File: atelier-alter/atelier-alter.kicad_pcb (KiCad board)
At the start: 2 copper layers, 81.3 x 80 mm, 59 parts, among them SW1 SW_DPST, SW2 SW_DPST, SW3 SW_DPST, SW4 RESET, U1 ATmega32U4-A, U2 PRTR5V0U2X, Y1 16Mhz

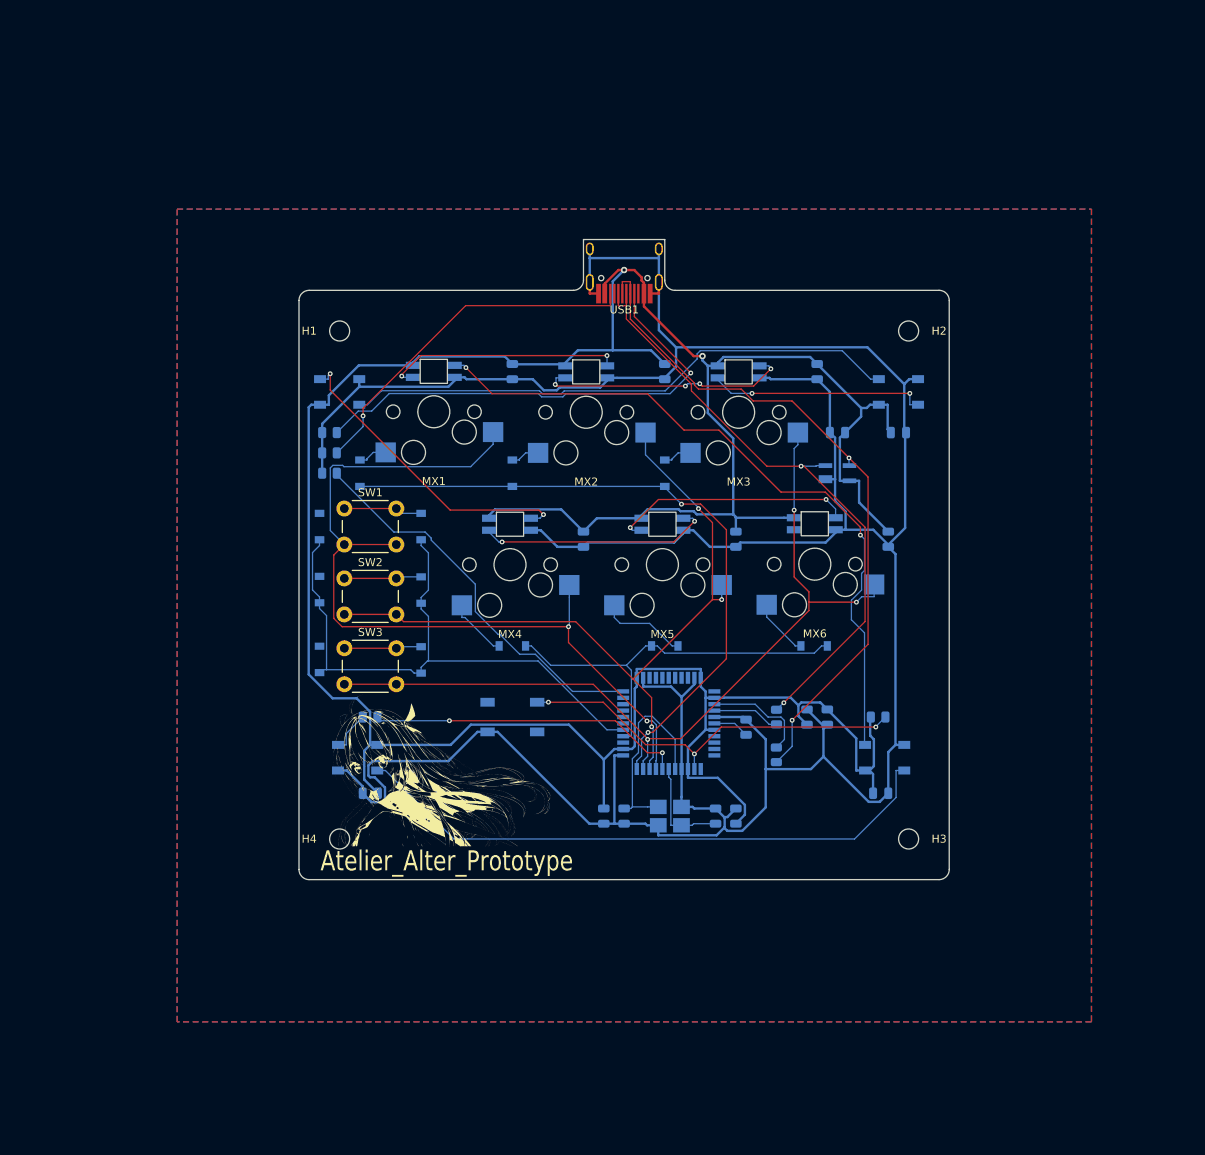
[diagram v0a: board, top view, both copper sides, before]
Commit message: small tweaks, done drawing the case
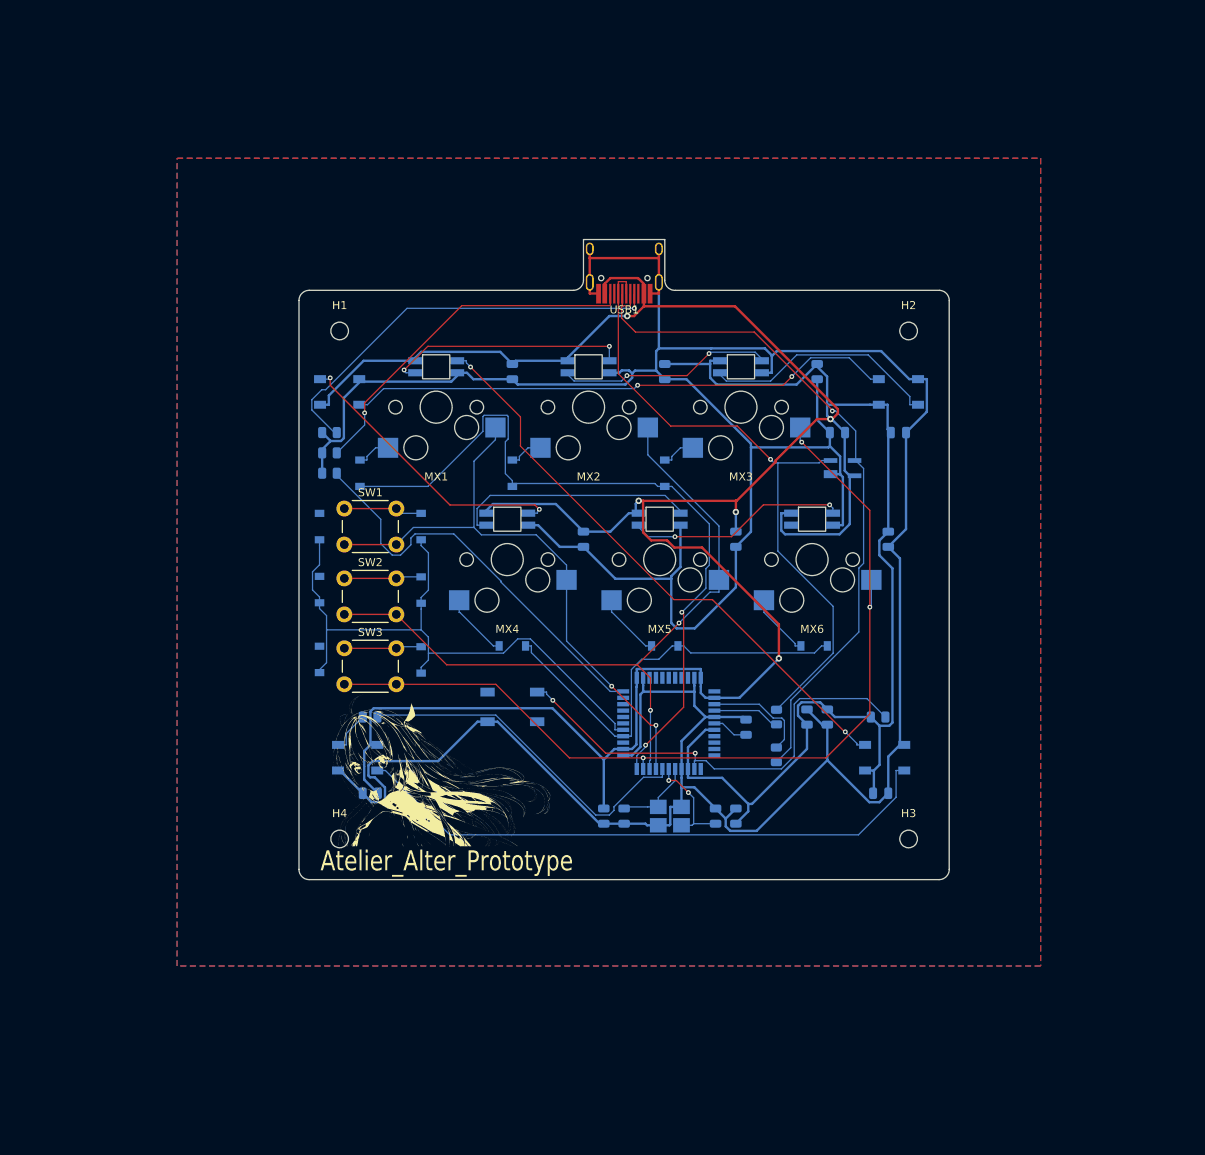
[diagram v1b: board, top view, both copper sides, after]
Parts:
- D14, D2, D5, D9: value SK6812 -> SK6812 / WS2812B; footprint LED_SMD:LED_SK6812_PLCC4_5.0x5.0mm_P3.2mm -> LED_SMD:LED_WS2812B_PLCC4_5.0x5.0mm_P3.2mm
- H1, H2, H3, H4: footprint MountingHole:MountingHole_2.5mm -> MountingHole:MountingHole_2.2mm_M2
- moved SW4 1.27 mm to (143.5, 113.0)
- moved U2 0.90 mm to (184.8, 83.2)
- moved MX4 0.72 mm to (142.9, 94.6)
- moved MX5 0.72 mm to (161.9, 94.6)
- moved MX3 0.70 mm to (172.1, 75.6)
- moved MX2 0.70 mm to (153.0, 75.6)
- moved MX6 0.67 mm to (181.0, 94.6)
- moved MX1 0.64 mm to (134.0, 75.6)
- turned D14 to 180 degrees
- turned D2 to 0 degrees
- turned D22 to 180 degrees
- turned D5 to 180 degrees
- turned D9 to 180 degrees
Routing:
- net +5V: track 378.2 -> 429.2 mm, vias 2 -> 5
- net COL1: track 107.6 -> 74.7 mm
- net GND: track 411.3 -> 443.9 mm
- net Net-(C3-Pad2): track 25.0 -> 9.96 mm
- net D11: track 87.9 -> 73.3 mm
- net COL3: track 104.7 -> 116.1 mm
- net ROW1: track 83.1 -> 93.9 mm
- net Net-(R4-Pad2): track 60.5 -> 52.4 mm
- net Net-(R3-Pad1): track 50.0 -> 57.7 mm, vias 3 -> 2
- net Net-(MX2-Pad3): track 31.9 -> 26.9 mm, vias 4 -> 2
- net RGB: track 39.5 -> 44.1 mm, vias 2 -> 0
- net D+: track 77.3 -> 81.9 mm, vias 2 -> 1
- net Net-(MX5-Pad3): track 30.3 -> 27.5 mm
- net Net-(D22-Pad2): track 11.0 -> 8.26 mm
- net ROW2: track 50.6 -> 53.2 mm
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
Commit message: minor updates here and there
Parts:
- removed D17, D18, D19: SOD-123, Diode_SMD:D_SOD-123
- H1, H2, H3, H4: footprint MountingHole:MountingHole_2.2mm_M2 -> MountingHole:MountingHole_5.3mm_M5
- moved R1 53.1 mm to (154.9, 70.5), turned to 0 degrees
- moved R2 46.9 mm to (159.7, 70.5), turned to 180 degrees
- moved R5 46.6 mm to (165.1, 67.3), turned to 90 degrees
- moved R6 45.5 mm to (154.9, 113.7), turned to 90 degrees
- moved U2 31.6 mm to (157.5, 67.3), turned to 180 degrees
- moved R4 31.4 mm to (149.9, 67.3), turned to 90 degrees
- moved D14 13.9 mm to (134.6, 67.9)
- moved D9 12.8 mm to (180.3, 67.9)
- moved Atorie' 12.1 mm to (146.7, 120.7)
- moved R7 12.0 mm to (129.3, 125.7)
- moved R3 11.4 mm to (185.4, 125.1)
- moved C10 8.76 mm to (134.3, 125.7)
- moved C11 8.67 mm to (181.0, 125.1), turned to 180 degrees
- moved D2 8.14 mm to (132.1, 121.3)
- moved SW4 7.43 mm to (146.1, 120.0)
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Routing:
- net GND: track 443.9 -> 371.1 mm
- net D-: track 87.2 -> 17.6 mm
- net D+: track 81.9 -> 13.3 mm
- net Net-(R6-Pad1): track 51.8 -> 2.49 mm
- net Net-(R3-Pad1): track 57.7 -> 106.6 mm, vias 2 -> 0
- net Net-(R2-Pad2): track 8.48 -> 53.7 mm, vias 0 -> 2
- net Net-(R1-Pad2): track 13.4 -> 52.9 mm, vias 0 -> 2
- net ROW3: track 78.3 -> 45.2 mm
- net Net-(R5-Pad2): track 44.9 -> 12.3 mm
- net Net-(R4-Pad2): track 52.4 -> 23.6 mm
- net Net-(D14-Pad2): track 68.5 -> 42.1 mm
- net Net-(D2-Pad4): track 74.5 -> 53.4 mm, vias 0 -> 2
- net ROW1: track 93.9 -> 73.7 mm, vias 2 -> 3
- net +5V: track 429.2 -> 442.5 mm, vias 5 -> 2
- net D12: track 29.9 -> 18.1 mm
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
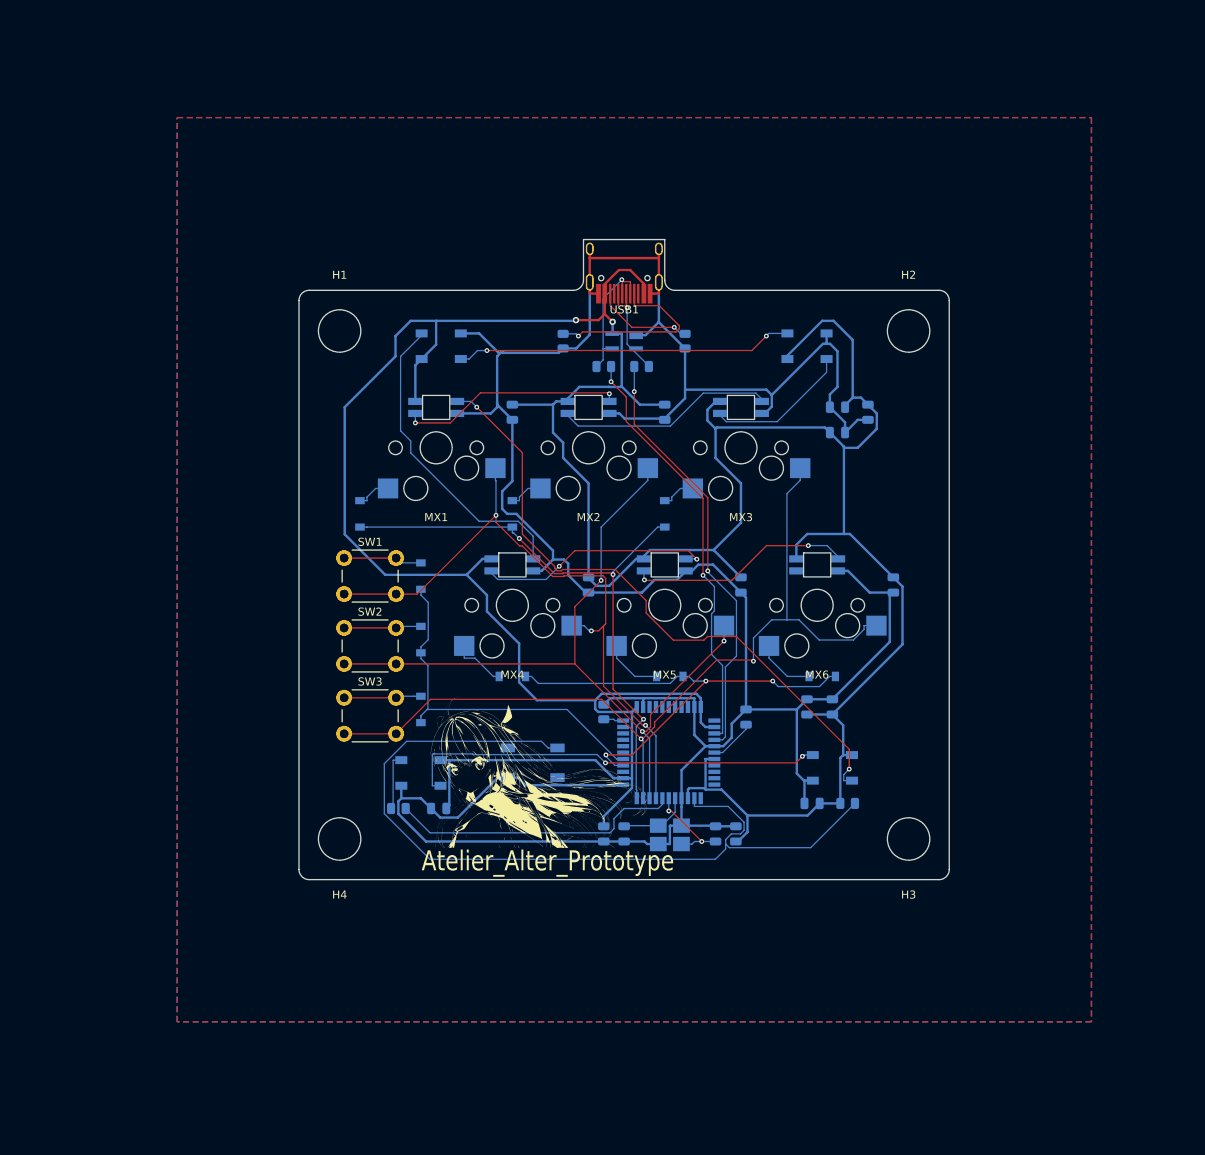
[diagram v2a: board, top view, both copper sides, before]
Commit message: decided to nuke all led capacitor
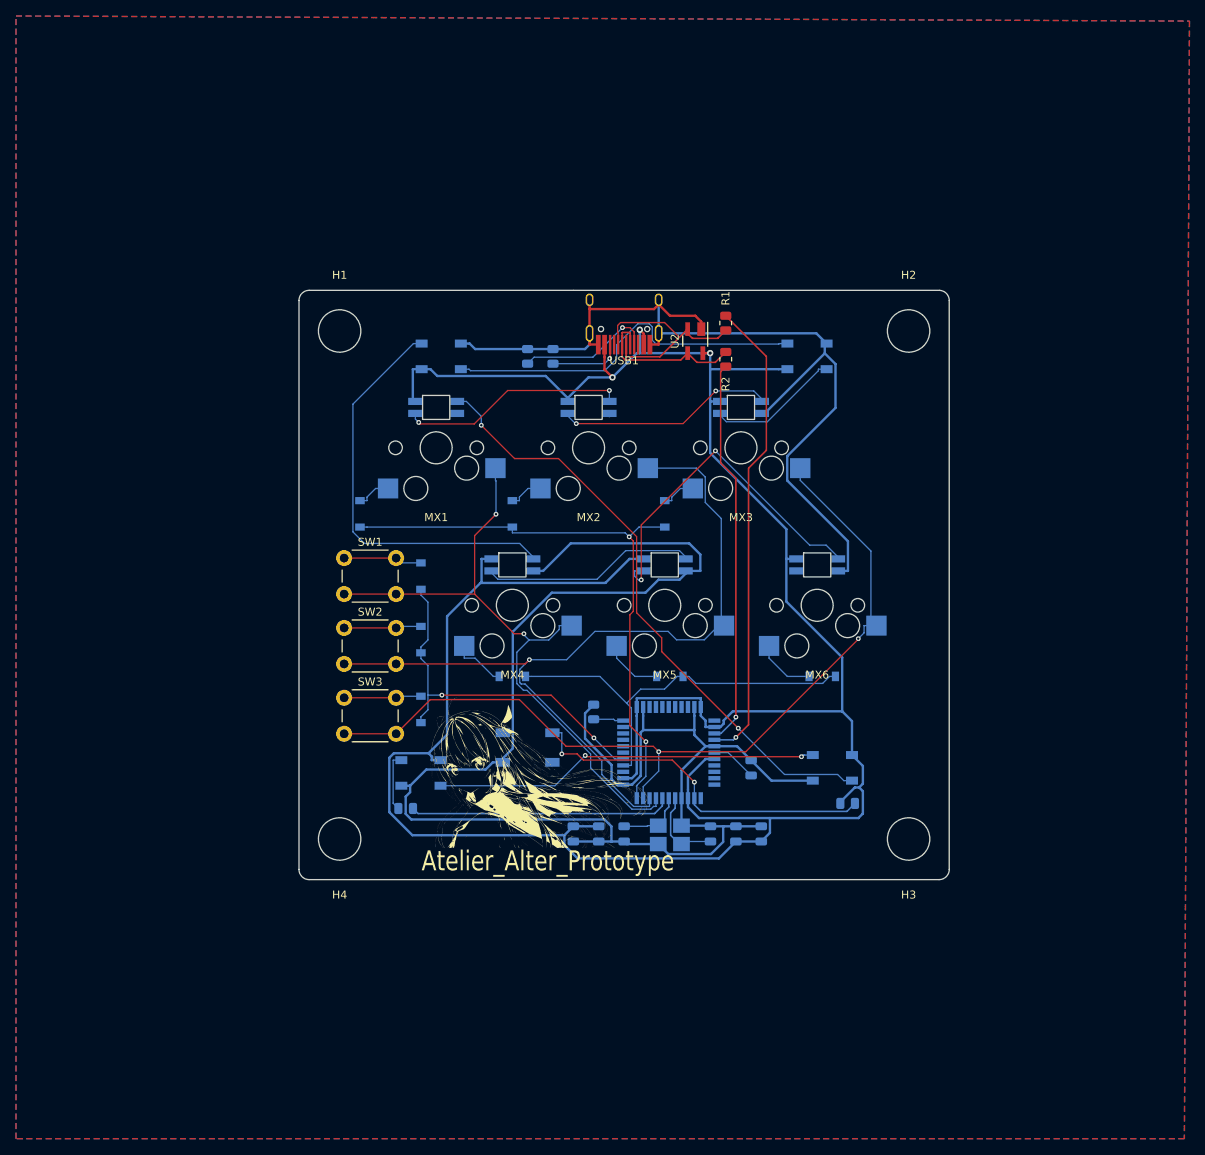
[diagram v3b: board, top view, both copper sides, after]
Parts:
- removed C10, C11, C12, C13, C14, C15, C16, C17, C8, C9: 100nF, Capacitor_SMD:C_0805_2012Metric
- R1, R2, U2: moved to F.Cu
- moved C7 33.2 mm to (151.1, 128.9), turned to -90 degrees
- moved C5 18.2 mm to (174.6, 128.9)
- moved R5 16.6 mm to (148.6, 69.2), turned to -90 degrees
- moved R1 15.3 mm to (170.2, 69.6), turned to -90 degrees
- moved R2 11.8 mm to (170.2, 65.0), turned to 90 degrees
- moved C2 11.4 mm to (157.5, 128.9), turned to 90 degrees
- moved C3 10.8 mm to (168.3, 128.9), turned to -90 degrees
- moved U2 8.89 mm to (166.4, 67.3), turned to -90 degrees
- moved C6 6.38 mm to (173.4, 120.7)
- moved USB1 6.37 mm to (157.5, 59.5)
- moved R4 4.84 mm to (145.4, 69.2), turned to -90 degrees
- moved SW4 2.01 mm to (145.4, 118.1)
- moved D14 1.27 mm to (134.6, 69.2)
- moved D9 1.27 mm to (180.3, 69.2)
- moved R6 1.27 mm to (153.7, 113.7)
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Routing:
- net +5V: track 442.5 -> 331.9 mm, vias 2 -> 3
- net Net-(R3-Pad1): track 106.6 -> 45.9 mm, vias 0 -> 2
- net GND: track 371.1 -> 327.4 mm
- net Net-(MX5-Pad3): track 28.0 -> 43.9 mm
- net D+: track 13.3 -> 27.6 mm, vias 1 -> 0
- net D21: track 39.0 -> 51.8 mm
- net COL2: track 95.5 -> 105.4 mm, vias 3 -> 1
- net ROW2: track 59.6 -> 51.3 mm, vias 3 -> 0
- net Net-(R4-Pad2): track 23.6 -> 17.0 mm
- net Net-(R2-Pad2): track 53.7 -> 59.2 mm, vias 2 -> 1
- net Net-(D2-Pad4): track 53.4 -> 48.3 mm
- net Net-(R1-Pad2): track 52.9 -> 48.5 mm, vias 2 -> 1
- net Net-(D14-Pad2): track 42.1 -> 46.4 mm, vias 2 -> 0
- net D11: track 79.8 -> 76.3 mm
- net Net-(R5-Pad2): track 12.3 -> 9.12 mm
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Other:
- board size 81.3 x 80 mm -> 81.3 x 73.7 mm

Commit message: update pcb + qmk firmware
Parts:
- removed the D2 at (132.1, 121.3)
- added D1: SK6812 / WS2812B, LED_SMD:LED_WS2812B_PLCC4_5.0x5.0mm_P3.2mm, B.Cu at (132.1, 121.9)
- added R8: 300, Resistor_SMD:R_0805_2012Metric, B.Cu at (153.0, 123.2)
- moved R7 24.1 mm to (153.0, 118.1), turned to -90 degrees
- moved R3 2.69 mm to (183.5, 127.0)
- moved R1 1.91 mm to (172.1, 69.6)
- moved R2 1.91 mm to (172.1, 65.0)
- moved U2 1.91 mm to (168.3, 67.3)
- moved D2 1.27 mm to (183.5, 121.9)
- moved R6 0.90 mm to (153.0, 113.0)
- renumbered D5 to D2, D9 to D3, D14 to D4
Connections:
- net RGB renamed Net-(R7-Pad1)
- D2 pad 4: D11 -> Net-(D2-Pad4)
- D3 pad 2: D12 -> Net-(D2-Pad4)
- D4 pad 4: D21 -> unconnected-(D4-Pad4)
- MX1 pad 2: D11 -> InKeyRGB
- MX4 pad 2: D21 -> D12
- R7 pad 2: Net-(D2-Pad2) -> InKeyRGB
- U1 pad 25: unconnected-(U1-Pad25) -> Net-(R8-Pad1)
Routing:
- net InKeyRGB: track 0.00 -> 92.3 mm
- net D11: track 76.3 -> 0.00 mm, vias 2 -> 0
- net Net-(D2-Pad4): track 0.00 -> 59.0 mm
- net D21: track 51.8 -> 0.00 mm
- net GND: track 327.4 -> 364.7 mm
- net +5V: track 331.9 -> 309.1 mm
- net D12: track 16.7 -> 36.8 mm
- net BackRGB: track 0.00 -> 18.7 mm
- net Net-(R7-Pad1): track 33.3 -> 14.7 mm, vias 0 -> 2
- net Net-(MX2-Pad3): track 27.4 -> 40.8 mm, vias 2 -> 0
- net Net-(D1-Pad4): track 48.3 -> 61.5 mm
- net Net-(MX5-Pad3): track 43.9 -> 33.0 mm
- net COL2: track 105.4 -> 95.9 mm, vias 1 -> 3
- net Net-(D2-Pad2): track 7.34 -> 0.00 mm
- net COL1: track 81.0 -> 74.0 mm
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
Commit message: final commit for rev 0.
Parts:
- H1, H2, H3, H4: footprint MountingHole:MountingHole_5.3mm_M5 -> MountingHole:MountingHole_3.2mm_M3_ISO7380
- R1, R2: footprint Resistor_SMD:R_0805_2012Metric -> Resistor_SMD:R_0603_1608Metric_Pad0.98x0.95mm_HandSolder
- SW1, SW2, SW3: footprint Button_Switch_THT:SW_PUSH_6mm_H9.5mm -> Button_Switch_THT:SW_PUSH_6mm_H13mm
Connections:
- U1 pad 25: Net-(R8-Pad1) -> unconnected-(U1-Pad25)
- U1 pad 28: unconnected-(U1-Pad28) -> Net-(R8-Pad1)
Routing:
- net Net-(R8-Pad1): track 4.80 -> 20.7 mm, vias 0 -> 2
- net InKeyRGB: track 92.3 -> 93.0 mm
